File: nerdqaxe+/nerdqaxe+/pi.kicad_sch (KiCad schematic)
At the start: 20 parts, among them J5 Conn_01x12-Socket, J6 Conn_01x12-Socket, J7 Conn_01x12-Header, J8 Conn_01x12-Header, M1 Fan_4pin, M2 Fan_4pin, U30 T-Display-S3, U32 EMC2302-1, U33 TXU0102-DCU, U37 TMP1075, U38 TMP1075

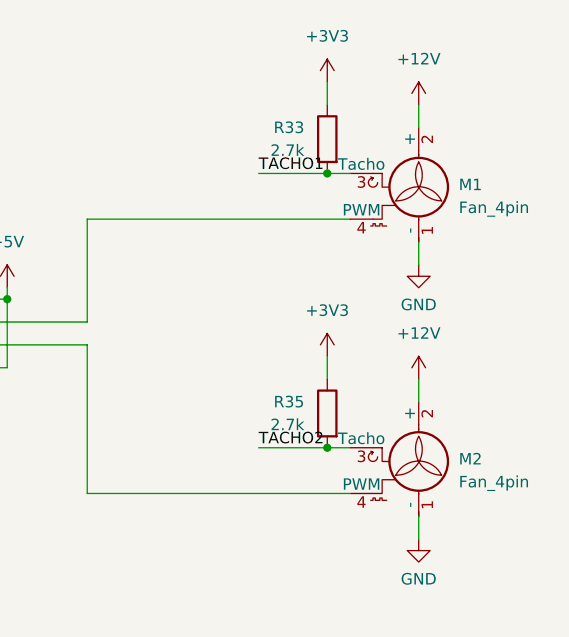
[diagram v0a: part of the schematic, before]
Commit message: updated bom of + for 24V cap
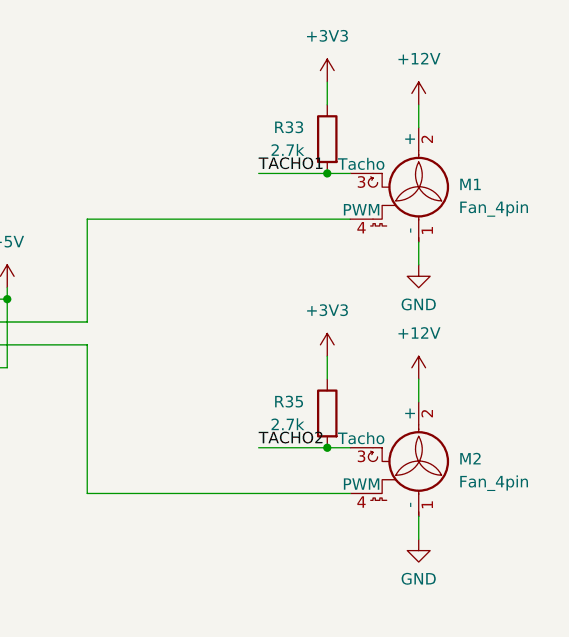
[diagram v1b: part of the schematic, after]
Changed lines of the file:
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@@
 (kicad_sch
-	(version 20231120)
+	(version 20250114)
 	(generator "eeschema")
-	(generator_version "8.0")
+	(generator_version "9.0")
 	(paper "A4")
+	(text "1x12 Socket for NerdQaxe+"
+		(exclude_from_sim no)
+		(at 29.21 179.07 0)
+		(effects
+			(font
+				(size 1.27 1.27)
+			)
+		)
+	)
+	(text "1x12 Pinheader for T-Display-S3"
+		(exclude_from_sim no)
+		(at 61.595 179.07 0)
+		(effects
+			(font
+				(size 1.27 1.27)
+			)
+		)
+	)
 	(junction
 		(at 220.345 131.445)
@@
 		)
 	)
-	(text "1x12 Socket for NerdQaxe+"
-		(exclude_from_sim no)
-		(at 29.21 179.07 0)
-		(effects
-			(font
-				(size 1.27 1.27)
-			)
-		)
-	)
-	(text "1x12 Pinheader for T-Display-S3"
-		(exclude_from_sim no)
-		(at 61.595 179.07 0)
-		(effects
-			(font
-				(size 1.27 1.27)
-			)
-		)
-	)
 	(label "SCL"
 		(at 201.295 53.975 0)
-		(fields_autoplaced yes)
 		(effects
 			(font
@@
 	(label "SDA"
 		(at 248.285 53.975 180)
-		(fields_autoplaced yes)
 		(effects
 			(font
@@
 	(label "SDA"
 		(at 139.065 128.905 180)
-		(fields_autoplaced yes)
 		(effects
 			(font
@@
 	(label "SCL"
 		(at 139.065 131.445 180)
-		(fields_autoplaced yes)
 		(effects
 			(font
@@
 	(label "TACHO1"
 		(at 174.625 139.065 0)
-		(fields_autoplaced yes)
 		(effects
 			(font
@@
 	(label "TACHO2"
 		(at 174.625 133.985 0)
-		(fields_autoplaced yes)
 		(effects
 			(font
@@
 	(label "TACHO2"
 		(at 248.285 147.955 0)
-		(fields_autoplaced yes)
 		(effects
 			(font
@@
 	(label "TACHO1"
 		(at 248.285 117.475 0)
-		(fields_autoplaced yes)
 		(effects
 			(font
@@
 		(shape bidirectional)
 		(at 154.305 76.835 0)
-		(fields_autoplaced yes)
 		(effects
 			(font
@@
 		(shape input)
 		(at 57.785 18.415 180)
-		(fields_autoplaced yes)
 		(effects
 			(font
@@
 		(shape output)
 		(at 97.79 79.375 180)
-		(fields_autoplaced yes)
 		(effects
 			(font
@@
 		(shape input)
 		(at 154.305 79.375 0)
-		(fields_autoplaced yes)
 		(effects
 			(font
@@
 		(shape input)
 		(at 103.505 99.695 180)
-		(fields_autoplaced yes)
 		(effects
 			(font
@@
 		(shape output)
 		(at 57.785 23.495 180)
-		(fields_autoplaced yes)
 		(effects
 			(font
@@
 		(shape output)
 		(at 154.305 74.295 0)
-		(fields_autoplaced yes)
 		(effects
 			(font
@@
 		(shape output)
 		(at 113.665 71.755 180)
-		(fields_autoplaced yes)
 		(effects
 			(font
@@
 		(shape input)
 		(at 57.785 20.955 180)
-		(fields_autoplaced yes)
 		(effects
 			(font
@@
 		(shape output)
 		(at 154.305 81.915 0)
-		(fields_autoplaced yes)
 		(effects
 			(font
@@
 		(shape output)
 		(at 110.49 86.995 180)
-		(fields_autoplaced yes)
 		(effects
 			(font
@@
 		(shape input)
 		(at 80.645 81.915 180)
-		(fields_autoplaced yes)
 		(effects
 			(font
@@
 		)
 	)
+	(embedded_fonts no)
 )
